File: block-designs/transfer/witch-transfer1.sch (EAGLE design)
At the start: 18 parts, among them IC1 74LS73N, IC2 74S08N

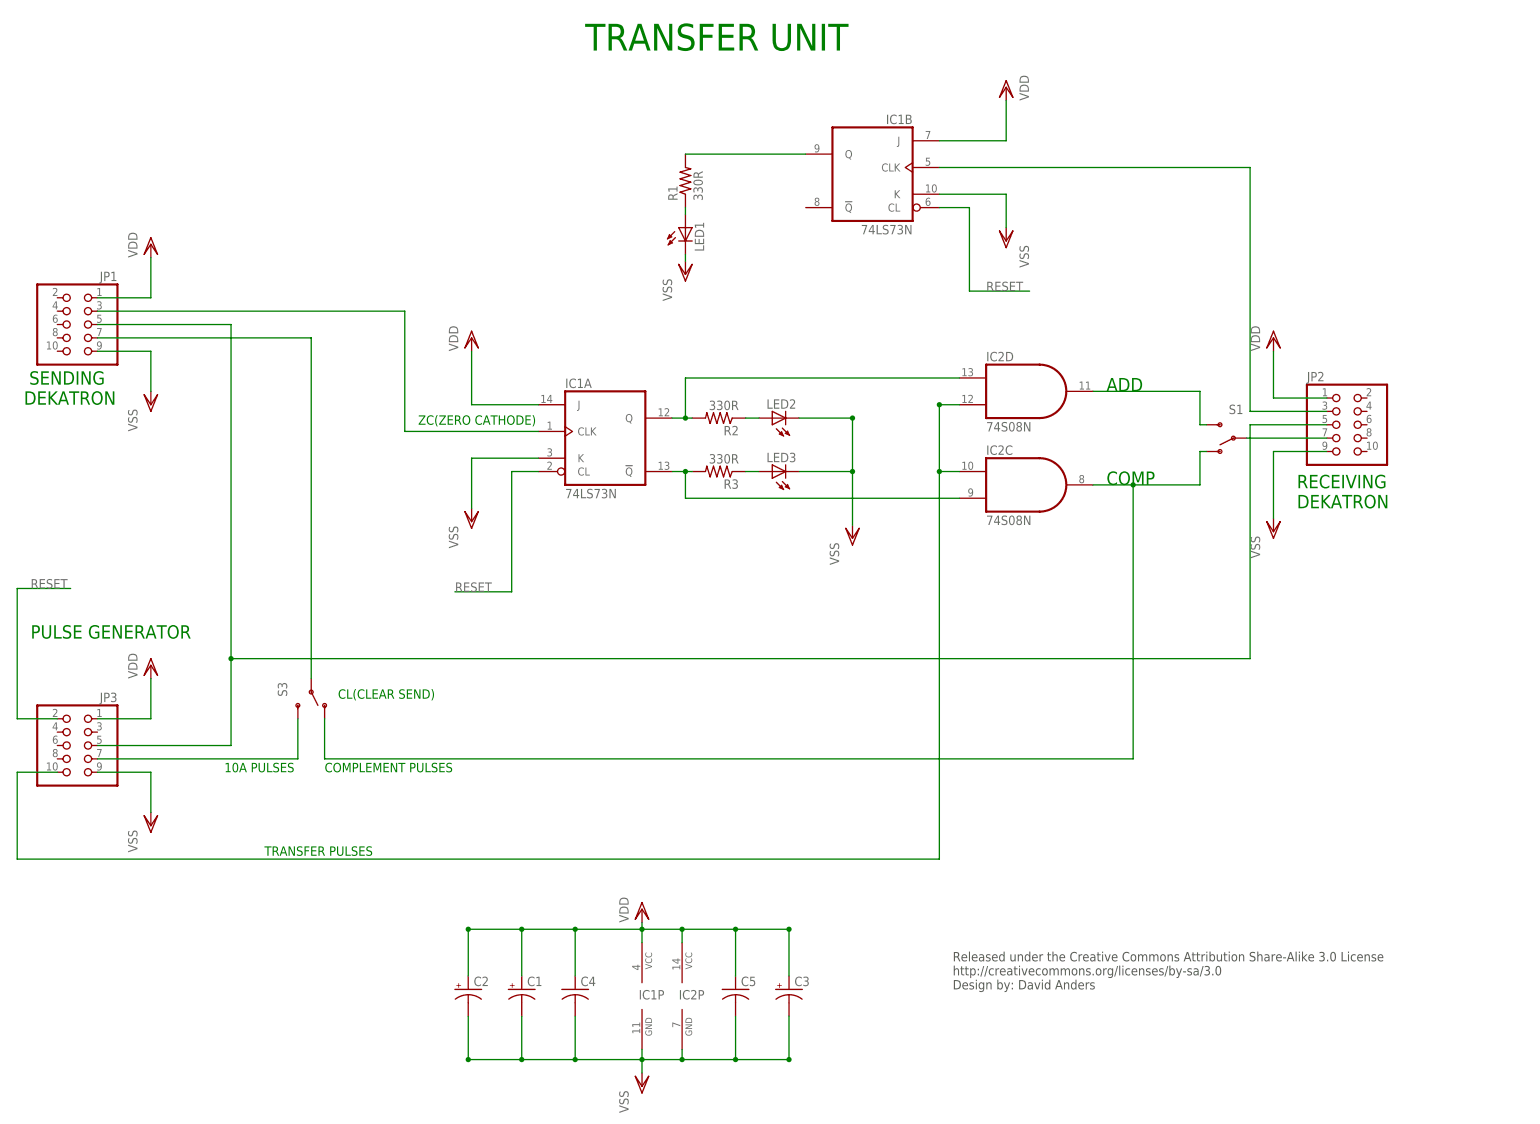
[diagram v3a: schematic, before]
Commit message: updated pdf schematics and board files with fixes
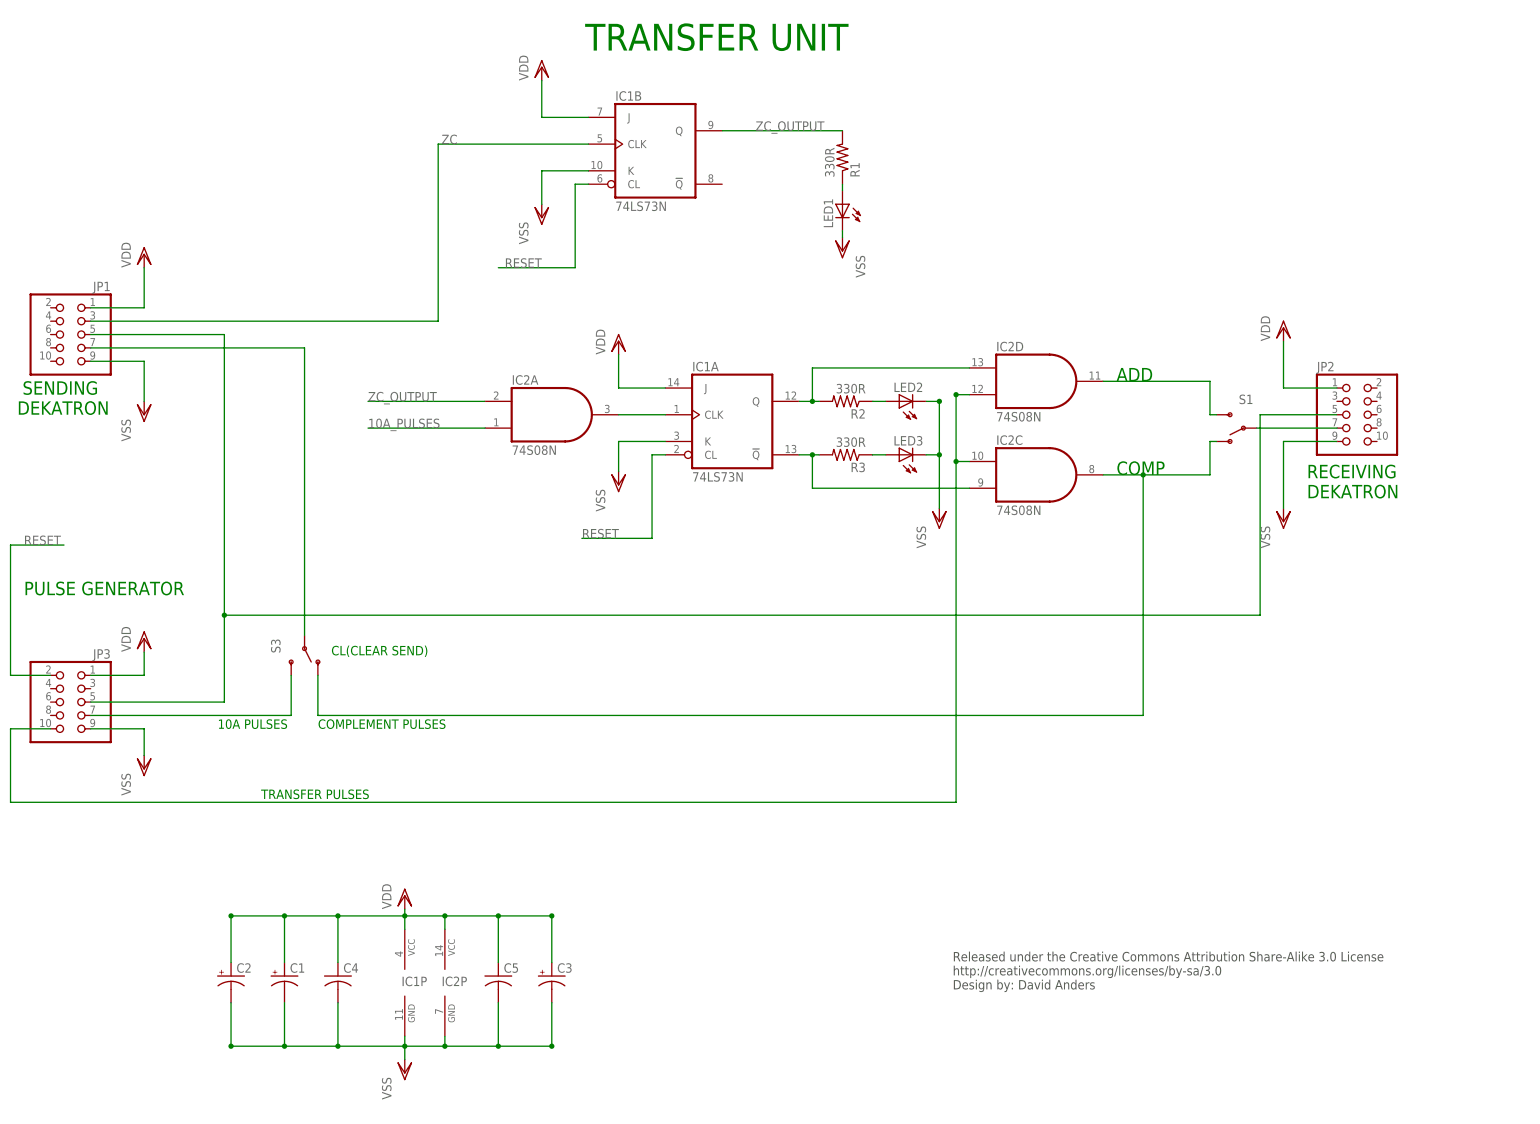
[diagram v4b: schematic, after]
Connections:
- removed net N$12: IC1B.Q, R1.2
- removed net N$9: JP3.7, S3.S
- removed net ZC_TX: IC1A.CLK, JP1.3
- new net 10A_PULSES: IC2A.I0, JP3.7, S3.S
- new net ZC: IC1B.CLK, JP1.3
- new net ZC_OUTPUT: IC1B.Q, IC2A.I1, R1.2
- net N$11: now also IC1A.CLK, IC2A.O; no longer IC1B.CLK, JP2.3
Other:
- note removed: "ZC(ZERO CATHODE)"
- moved on the sheet: C1, C2, C3, C4, C5, IC1A, IC1B, IC1P, IC2C, IC2D, IC2P, JP1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
